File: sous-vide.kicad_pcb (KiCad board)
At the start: 2 copper layers, 95 x 68 mm, 25 parts, among them J1 Conn_01x02, J2 Conn_01x02, J3 Conn_01x02, Q1 2N3904, SW1 SW_Push_Dual, SW2 SW_Push_Dual, U1 G5LE, U2 RAC01, U3 node_mcu1.0, U4 P090S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

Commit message: add filter capacitor to thermistor
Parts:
- added C1: C, Capacitors_THT:C_Disc_D4.3mm_W1.9mm_P5.00mm, F.Cu at (193.0, 102.0)
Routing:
- net /THERMISTOR: track 30.6 -> 44.6 mm
- net Net-(C1-Pad2): track 21.9 -> 30.5 mm

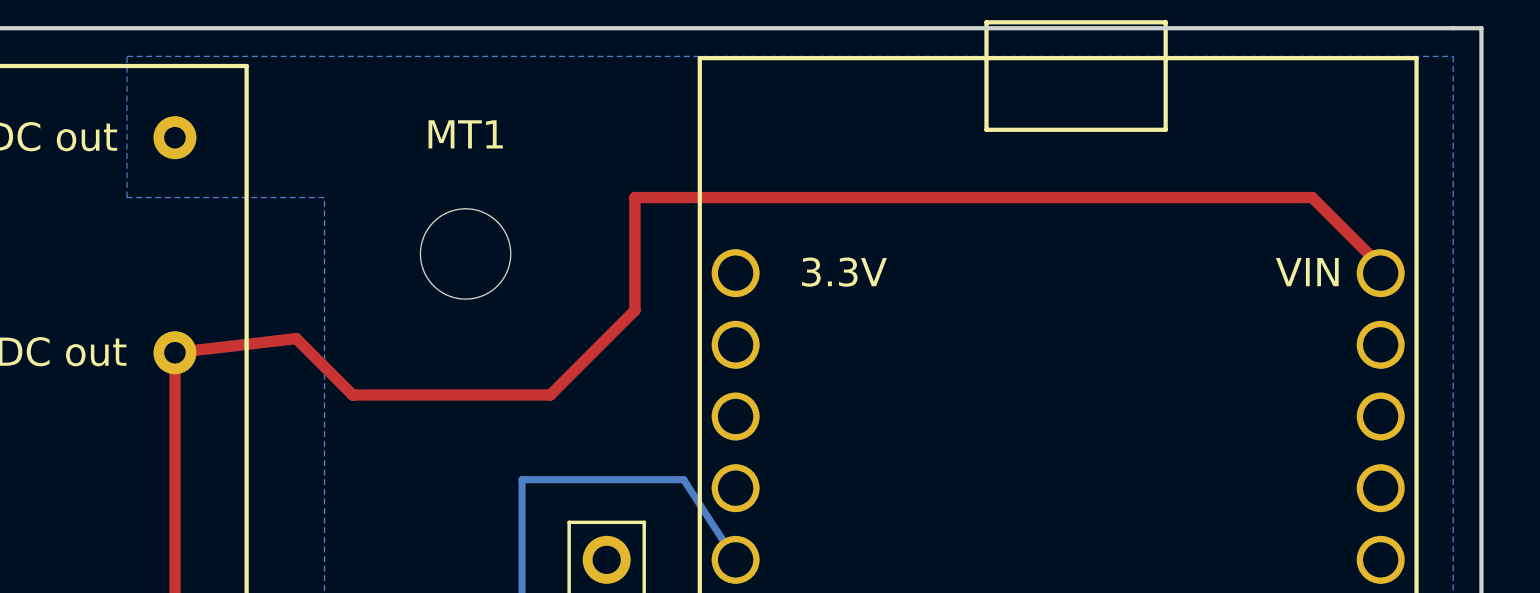
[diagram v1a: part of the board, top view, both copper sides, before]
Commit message: tested analog-multiplexor circuit
 - it works!
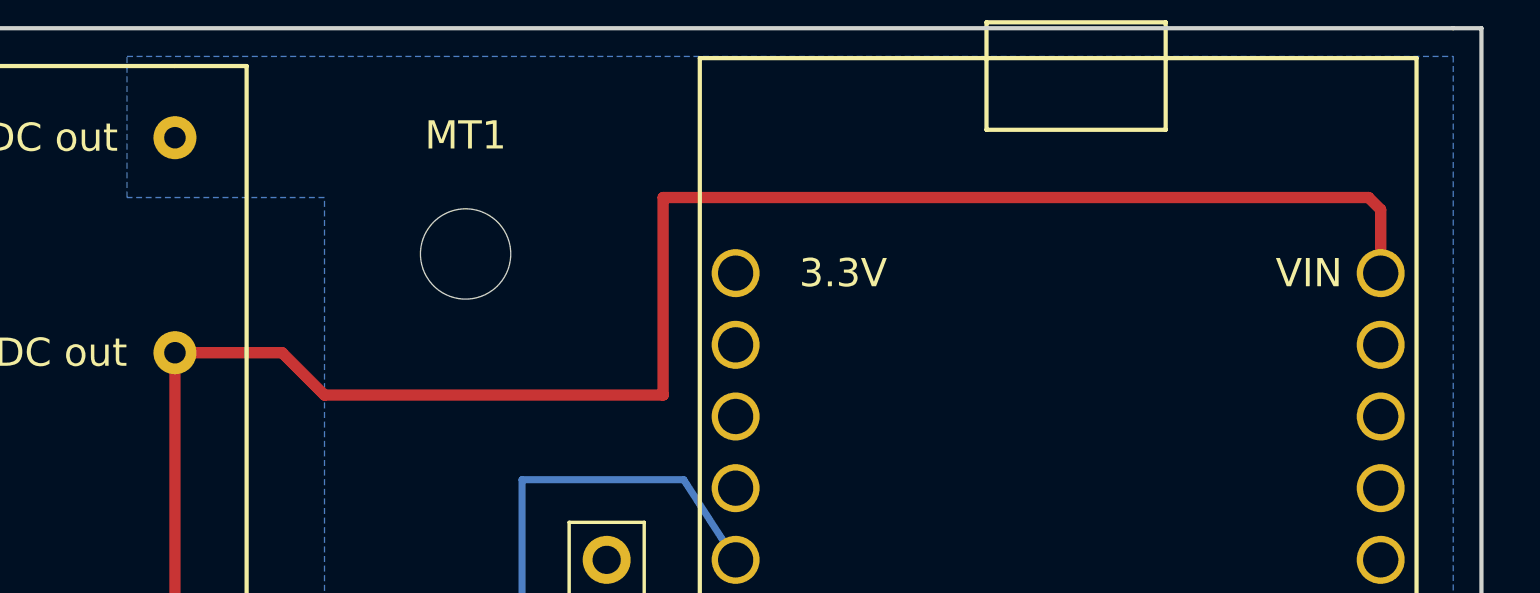
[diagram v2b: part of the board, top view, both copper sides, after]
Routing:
- net +5V: track 105.9 -> 108.8 mm
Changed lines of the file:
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@@
     (links 47)
     (no_connects 0)
-    (area 104.550999 34.214999 205.04762 107.635)
+    (area 105.924999 36.924999 201.075001 105.075001)
     (thickness 1.6)
     (drawings 87)
@@
   (segment (start 156.27 74.27) (end 158 76) (width 0.25) (layer F.Cu) (net 8))
   (segment (start 151.54 74) (end 151.27 74.27) (width 0.25) (layer F.Cu) (net 8) (status 30))
-  (segment (start 154.7 48.5) (end 159 48) (width 0.4) (layer F.Cu) (net 10) (status 10))
-  (segment (start 195 43) (end 197.43 45.43) (width 0.4) (layer F.Cu) (net 10) (status 20))
-  (segment (start 171 43) (end 195 43) (width 0.4) (layer F.Cu) (net 10))
-  (segment (start 171 47) (end 171 43) (width 0.4) (layer F.Cu) (net 10))
-  (segment (start 168 50) (end 171 47) (width 0.4) (layer F.Cu) (net 10))
-  (segment (start 161 50) (end 168 50) (width 0.4) (layer F.Cu) (net 10))
-  (segment (start 159 48) (end 161 50) (width 0.4) (layer F.Cu) (net 10))
+  (segment (start 154.7 48.5) (end 158.5 48.5) (width 0.4) (layer F.Cu) (net 10) (status 400000))
+  (segment (start 197.43 43.43) (end 197.43 45.68) (width 0.4) (layer F.Cu) (net 10) (status 800000))
+  (segment (start 197 43) (end 197.43 43.43) (width 0.4) (layer F.Cu) (net 10))
+  (segment (start 172 43) (end 197 43) (width 0.4) (layer F.Cu) (net 10))
+  (segment (start 172 50) (end 172 43) (width 0.4) (layer F.Cu) (net 10))
+  (segment (start 160 50) (end 172 50) (width 0.4) (layer F.Cu) (net 10))
+  (segment (start 158.5 48.5) (end 160 50) (width 0.4) (layer F.Cu) (net 10))
   (segment (start 197.43 45.43) (end 197.43 45.68) (width 0.4) (layer F.Cu) (net 10) (status 30))
   (segment (start 166 65) (end 166 63) (width 0.4) (layer F.Cu) (net 10) (status 10))

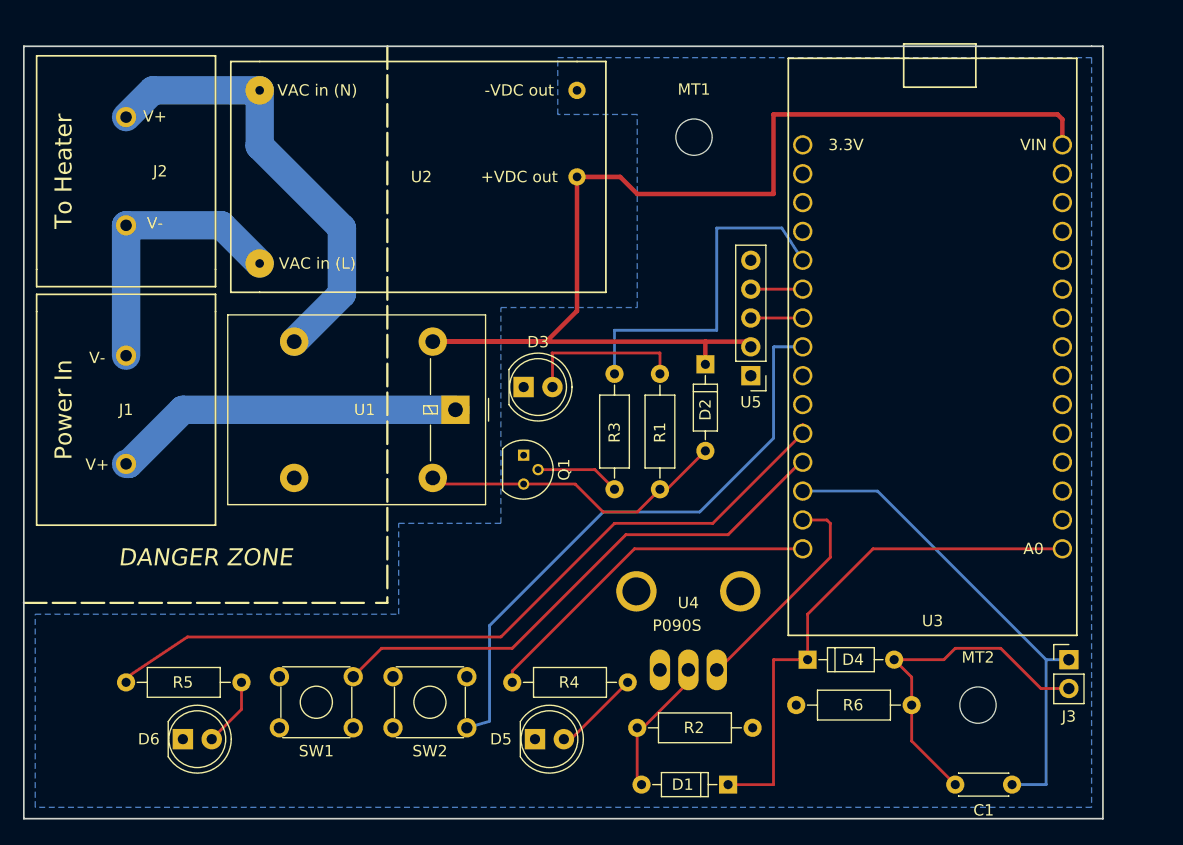
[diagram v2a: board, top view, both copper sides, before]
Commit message: thermistor test "works"
 - if I understand correctly, R_Ref is calculated to be 1.1k
 - works for the one sample (Temp, ADC) I have
 - removed the 1k resistor on the relay circuit
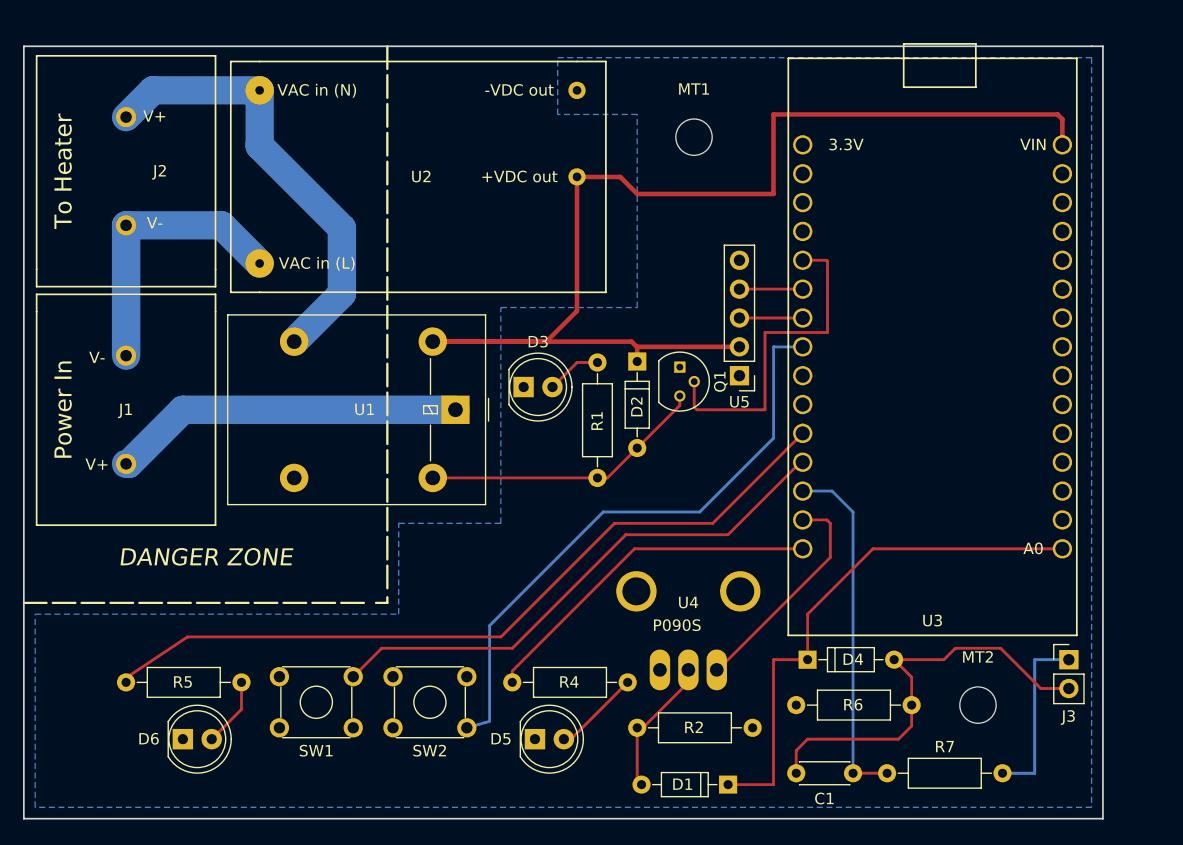
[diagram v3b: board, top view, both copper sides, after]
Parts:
- removed R3: 1.1k, Resistors_THT:R_Axial_DIN0207_L6.3mm_D2.5mm_P10.16mm_Horizontal
- added R7: 1.1k, Resistors_THT:R_Axial_DIN0207_L6.3mm_D2.5mm_P10.16mm_Horizontal, F.Cu at (182.0, 101.0)
- C1: value C -> 200nF
- moved Q1 15.8 mm to (163.8, 65.2)
- moved C1 14.0 mm to (179.0, 101.0)
- moved D2 6.01 mm to (160.0, 64.8)
- moved R1 5.59 mm to (156.5, 75.0)
- moved U5 1.00 mm to (169.0, 66.0)
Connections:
- J3 pad 1: /THERMISTOR -> Net-(J3-Pad1)
- U3 pad 26: Net-(R3-Pad2) -> Net-(Q1-Pad2)
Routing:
- net Net-(R3-Pad2): track 30.5 -> 0.00 mm
- net Net-(Q1-Pad2): track 7.83 -> 29.4 mm
- net Net-(J3-Pad1): track 0.00 -> 15.8 mm
- net /THERMISTOR: track 44.6 -> 31.2 mm
- net Net-(D3-Pad2): track 14.4 -> 4.85 mm
- net Net-(C1-Pad2): track 30.5 -> 36.8 mm
- net Net-(D2-Pad2): track 28.0 -> 25.2 mm
- net +5V: track 108.8 -> 107.1 mm
- net /DAT: track 4.57 -> 5.57 mm
- net /CLK: track 4.57 -> 5.57 mm

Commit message: ready for Fab!
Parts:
- added J4: Jumper, Pin_Headers:Pin_Header_Straight_1x02_Pitch2.54mm, F.Cu at (161.0, 54.5)
- added J5: Jumper, Pin_Headers:Pin_Header_Straight_1x02_Pitch2.54mm, F.Cu at (161.0, 58.5)
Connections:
- D2 pad 1: +5V -> Net-(D2-Pad1)
- U1 pad 2: +5V -> Net-(D2-Pad1)
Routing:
- net +5V: track 107.1 -> 68.0 mm
- net Net-(D2-Pad1): track 0.00 -> 36.9 mm
- net Net-(J5-Pad2): track 29.4 -> 38.0 mm

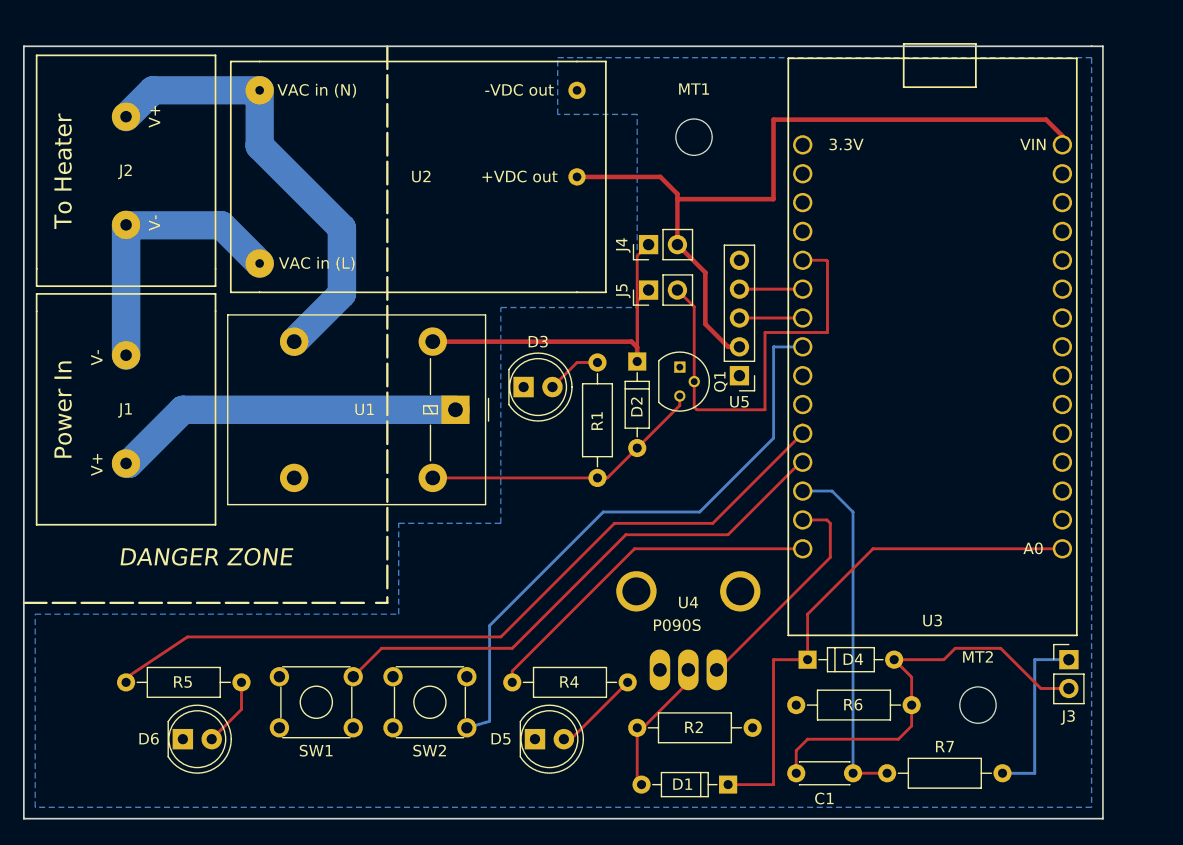
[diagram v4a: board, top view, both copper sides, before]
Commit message: V 0.3
 - added protection circuit and fuse
 - fixed LED indicator on relay circuit with Jeff's help
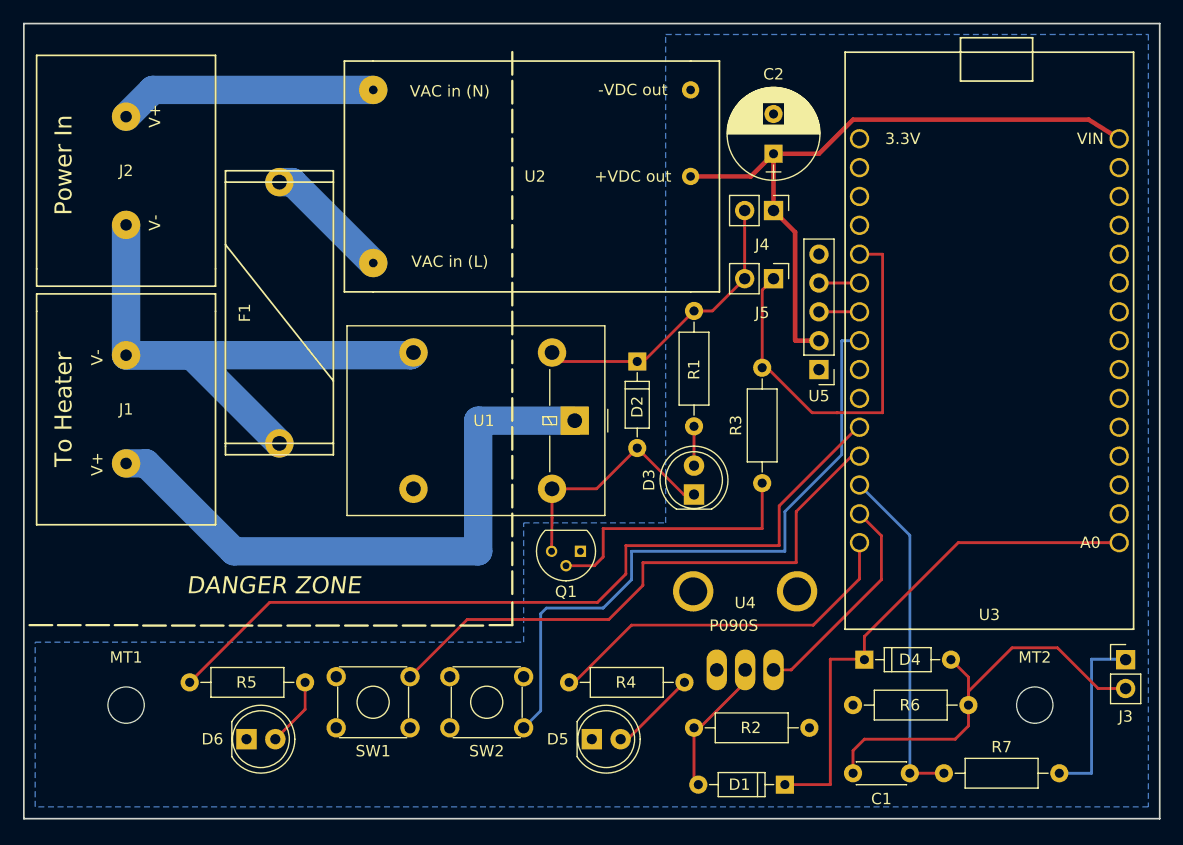
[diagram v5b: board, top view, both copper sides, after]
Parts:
- added C2: 330uF, Capacitors_THT:CP_Radial_D8.0mm_P3.50mm, F.Cu at (172.0, 46.5)
- added F1: Fuse, custom:Fuse_Holder_65600001009, F.Cu at (128.5, 60.5)
- added R3: 500, Resistors_THT:R_Axial_DIN0207_L6.3mm_D2.5mm_P10.16mm_Horizontal, F.Cu at (171.0, 75.5)
- moved MT1 70.7 mm to (115.0, 95.0)
- moved Q1 18.4 mm to (155.0, 81.5), turned to 180 degrees
- moved D3 17.7 mm to (165.0, 76.5), turned to 90 degrees
- moved J4 11.4 mm to (172.0, 51.5), turned to 270 degrees
- moved J5 11.0 mm to (172.0, 57.5), turned to 270 degrees
- moved U1 10.5 mm to (154.5, 70.0)
- moved U2 10.0 mm to (152.0, 48.5)
- moved R1 9.64 mm to (165.0, 70.5)
- moved U5 7.02 mm to (176.0, 65.5)
- moved D6 5.60 mm to (125.6, 98.0)
- moved R5 5.60 mm to (120.6, 93.0)
- moved U3 5.03 mm to (191.0, 65.5)
- moved C1 5.00 mm to (184.0, 101.0)
- moved D1 5.00 mm to (173.0, 102.0)
- moved D4 5.00 mm to (180.0, 91.0)
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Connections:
- D3 pad 1: GND -> Net-(D2-Pad2)
- J1 pad 2: Net-(J1-Pad2) -> Net-(F1-Pad2)
- J2 pad 2: Net-(J1-Pad2) -> Net-(F1-Pad2)
- J4 pad 1: Net-(D2-Pad1) -> +5V
- J4 pad 2: +5V -> Net-(D2-Pad1)
- J5 pad 1: Net-(D2-Pad1) -> Net-(J5-Pad1)
- J5 pad 2: Net-(J5-Pad2) -> Net-(D2-Pad1)
- Q1 pad 2: Net-(J5-Pad2) -> Net-(Q1-Pad2)
- R1 pad 1: Net-(D2-Pad2) -> Net-(D3-Pad2)
- R1 pad 2: Net-(D3-Pad2) -> Net-(D2-Pad1)
- U1 pad 3: Net-(J2-Pad1) -> Net-(F1-Pad2)
- U2 pad 2: Net-(J1-Pad2) -> Net-(F1-Pad1)
- U3 pad 26: Net-(J5-Pad2) -> Net-(J5-Pad1)
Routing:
- net Net-(F1-Pad2): track 0.00 -> 53.8 mm
- net Net-(J5-Pad2): track 38.0 -> 0.00 mm
- net Net-(J5-Pad1): track 0.00 -> 36.7 mm
- net Net-(J1-Pad2): track 24.9 -> 0.00 mm
- net Net-(Q1-Pad2): track 0.00 -> 24.1 mm
- net Net-(J1-Pad1): track 31.0 -> 54.2 mm
- net Net-(J2-Pad1): track 39.6 -> 22.7 mm
- net Net-(F1-Pad1): track 0.00 -> 11.2 mm
- net Net-(D2-Pad1): track 36.9 -> 26.3 mm
- net +5V: track 68.0 -> 59.6 mm
- net /SW2: track 52.9 -> 58.1 mm
- net /SW1: track 47.4 -> 51.4 mm
- net Net-(D2-Pad2): track 25.2 -> 21.9 mm
- net /BLUE_LED: track 68.9 -> 71.8 mm
- net /DAT: track 5.57 -> 3.57 mm
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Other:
- board size 95 x 68 mm -> 100 x 70 mm

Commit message: fix power circuit
 - reroute
 - make board slightly bigger
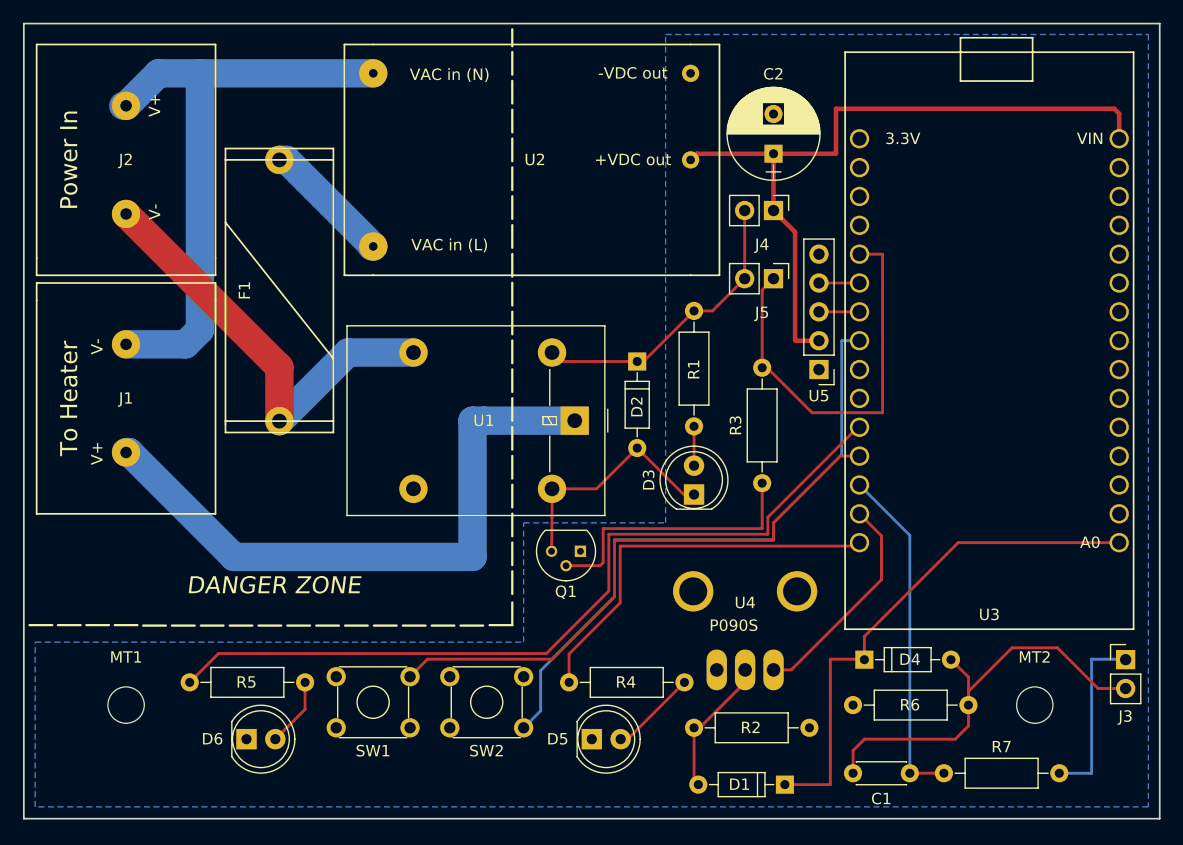
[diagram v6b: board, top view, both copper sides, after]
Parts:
- J1: value Conn_01x02 -> Heater
- J2: value Conn_01x02 -> Power
- moved F1 1.96 mm to (128.5, 58.5)
- moved U2 1.46 mm to (152.0, 47.0)
- moved J2 0.96 mm to (115.0, 47.0)
- moved J1 0.96 mm to (115.0, 68.0)
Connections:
- net Net-(D2-Pad1) renamed /+coil
- net Net-(D2-Pad2) renamed /-coil
- net Net-(J5-Pad1) renamed /Relay
- J1 pad 2: Net-(F1-Pad2) -> Net-(J1-Pad2)
- J2 pad 1: Net-(J2-Pad1) -> Net-(J1-Pad2)
- U2 pad 1: Net-(J2-Pad1) -> Net-(J1-Pad2)
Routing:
- net Net-(J1-Pad2): track 0.00 -> 52.8 mm
- net Net-(J2-Pad1): track 22.7 -> 0.00 mm
- net Net-(F1-Pad2): track 53.8 -> 38.1 mm
- net +5V: track 59.6 -> 63.6 mm
- net /SW2: track 58.1 -> 55.4 mm
- net /RED_LED: track 32.6 -> 35.1 mm
- net Net-(J1-Pad1): track 54.2 -> 55.3 mm
